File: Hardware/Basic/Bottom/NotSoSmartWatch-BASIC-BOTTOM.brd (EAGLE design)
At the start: 33 x 33 mm, 31 parts, among them U1 AD5242-SO16

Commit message: updated partially through Take 003
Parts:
- added J1: (no value), LinnesLab-Connectors:1X07
- moved R19 53.6 mm to (10.1, -22.2)
- moved R15 53.2 mm to (31.4, -19.7)
- moved R14 52.3 mm to (5.68, -21.0)
- moved C11 50.7 mm to (16.2, -20.1), turned to 90 degrees
- moved R13 50.6 mm to (10.8, -17.4)
- moved IMU1 50.1 mm to (45.1, 40.2)
- moved C1 49.8 mm to (39.9, 40.1)
- moved R21 48.9 mm to (37.3, -17.2)
- moved C14 44.1 mm to (4.16, -12.6)
- moved R17 42.8 mm to (30.3, -6.71)
- moved R18 42.5 mm to (30.3, -8.06), turned to 180 degrees
- moved R20 42.2 mm to (4.85, -15.9)
- moved C16 41.8 mm to (27.8, -16.4)
- moved R22 36.9 mm to (29.9, -12.8), turned to 90 degrees
- moved C15 36.1 mm to (16.1, -16.0)
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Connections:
- removed net LED.CTRL: U$4.8
- removed net PPG: C21.2, OP3.1, U1.14
- removed net TIA: C10.2, C15.1, OP4.1, U1.3
- new net A6/TIA: C10.2, C15.1, J1.5, OP4.1, U1.3
- new net A7/PPG: C21.2, J1.7, OP3.1, U1.14
- new net D29/LED.CTRL: J1.6, U$4.8
- net 3.3V: now also J1.2
- net GND: now also J1.1
- net SCL: now also J1.3
- net SDA: now also J1.4
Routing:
- net N$19: track 0.00 -> 18.4 mm
- net G.W2: track 0.00 -> 4.17 mm
- net N$10: track 0.00 -> 3.96 mm
- net GND: track 0.00 -> 3.96 mm, vias 0 -> 2
- net A7/PPG: track 0.00 -> 2.45 mm
- net N$20: track 0.00 -> 1.75 mm
- net VREF: track 0.00 -> 1.27 mm
- added copper zone on layer 16, net GND

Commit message: still working through Take 003
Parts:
- J1: device LinnesLab-Connectors:1X07 -> LinnesLab-Connectors:1X07_1.27MM
- moved R19 42.1 mm to (32.2, 13.6), turned to 270 degrees
- moved R21 41.5 mm to (26.7, 23.0)
- moved R15 41.0 mm to (26.7, 21.0), turned to 180 degrees
- moved IMU1 40.6 mm to (6.54, 27.4), turned to 90 degrees
- moved R14 38.1 mm to (29.6, 8.63), turned to 0 degrees
- moved C1 37.6 mm to (6.37, 23.0), turned to 0 degrees
- moved R23 35.7 mm to (30.0, 22.4), turned to 180 degrees
- moved R13 35.4 mm to (32.3, 10.7)
- moved C16 35.0 mm to (26.6, 18.5)
- moved U1 33.9 mm to (11.1, 9.05)
- moved C19 33.4 mm to (30.0, 20.5), turned to 180 degrees
- moved C18 33.1 mm to (5.85, 8.44), turned to 270 degrees
- moved R20 32.5 mm to (29.7, 5.13), turned to 180 degrees
- moved C14 32.1 mm to (29.6, 6.91), turned to 180 degrees
- moved R22 31.4 mm to (30.0, 18.6), turned to 0 degrees
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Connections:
- net 3.3V: now also J1.4; no longer J1.2
- net GND: now also J1.3; no longer J1.1
- net SCL: now also J1.2; no longer J1.3
- net SDA: now also J1.1; no longer J1.4
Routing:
- net A6/TIA: track 0.00 -> 39.3 mm, vias 0 -> 2
- net PD.C: track 0.00 -> 25.8 mm, vias 0 -> 2
- net GND: track 3.96 -> 19.1 mm, vias 2 -> 9
- net A7/PPG: track 2.45 -> 16.1 mm
- net G.W2: track 4.17 -> 15.7 mm, vias 0 -> 2
- net N$13: track 0.00 -> 11.4 mm
- net N$17: track 0.00 -> 6.83 mm
- net N$18: track 0.00 -> 6.40 mm
- net N$15: track 0.00 -> 5.91 mm
- net N$19: track 18.4 -> 22.8 mm
- net N$16: track 0.00 -> 4.20 mm
- net LED.C: track 0.00 -> 3.80 mm
- net SCL: track 0.00 -> 3.64 mm
- net SDA: track 0.00 -> 3.12 mm

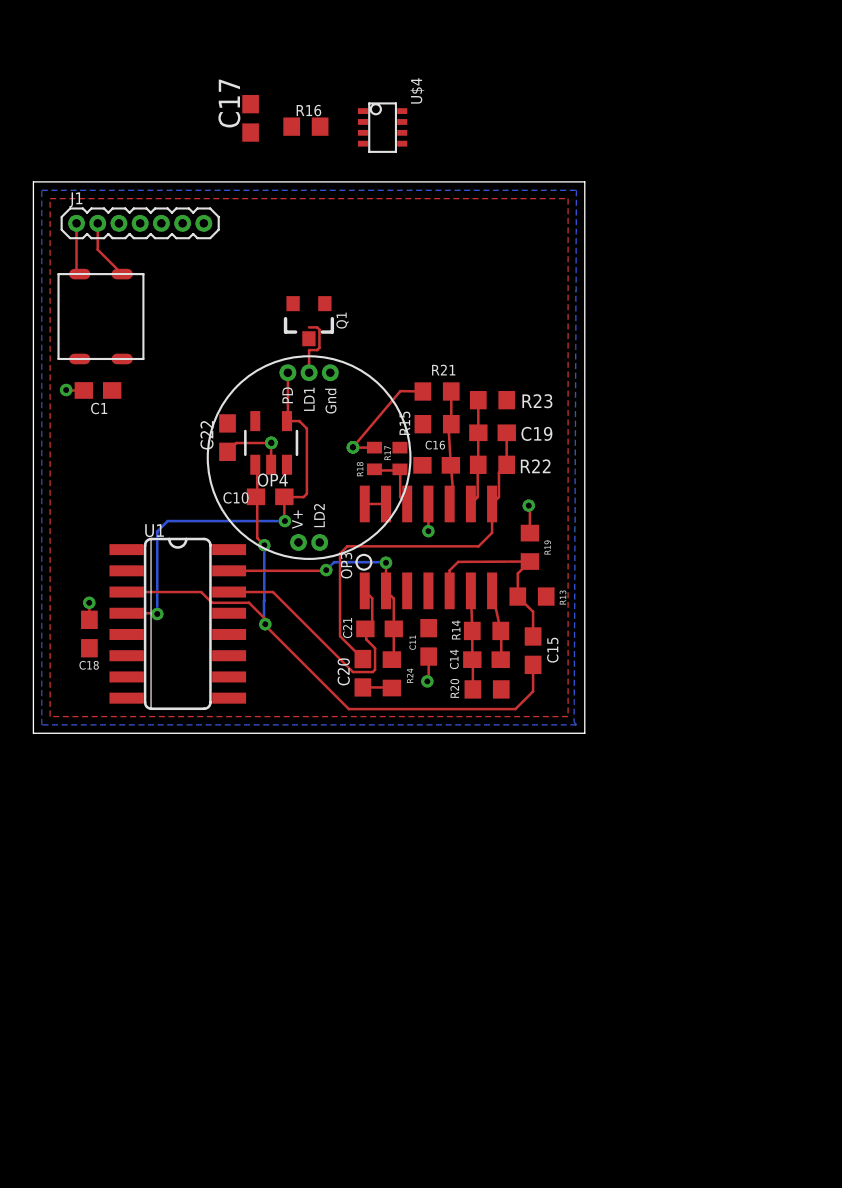
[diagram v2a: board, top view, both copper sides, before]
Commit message: updated through Take 003 - worried I might have isolated polygon
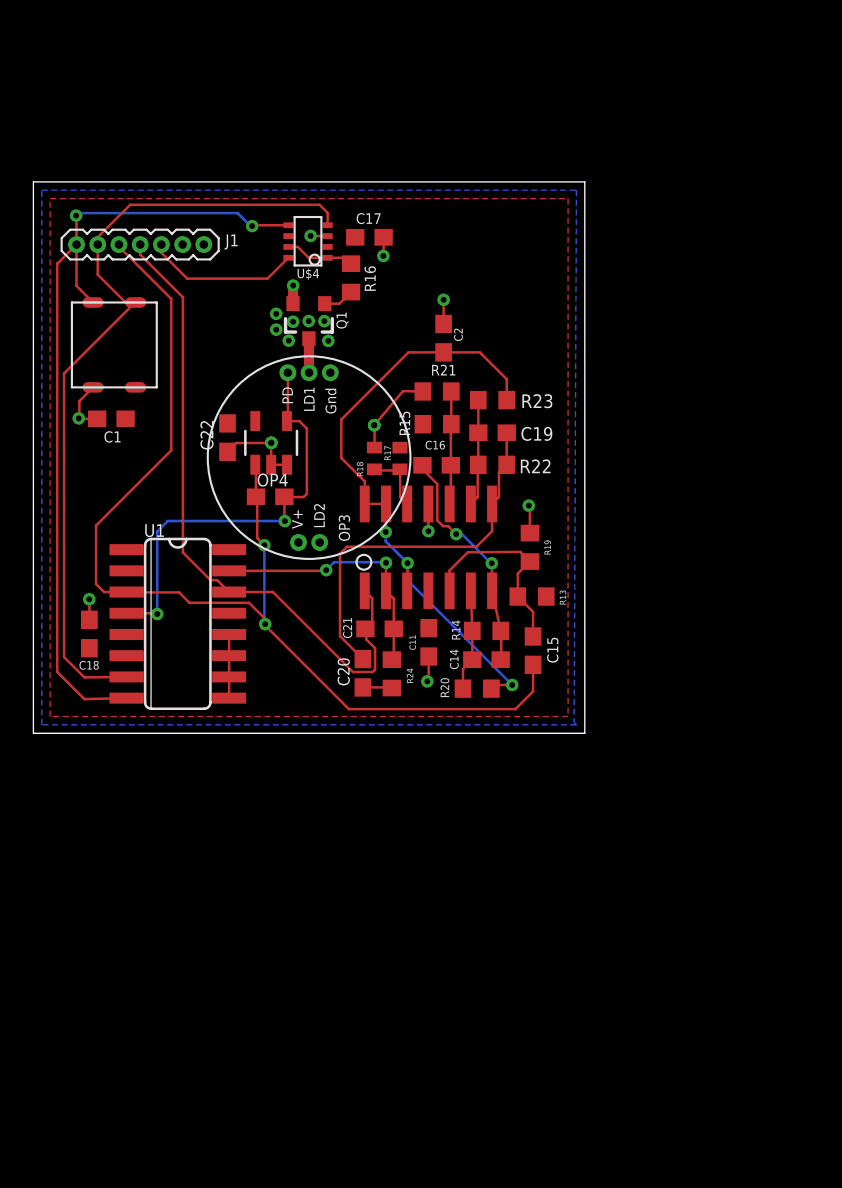
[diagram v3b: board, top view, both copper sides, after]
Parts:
- added C2: 100n, LinnesLab-Passives:C0603
- moved C17 10.1 mm to (22.6, 32.2), turned to 180 degrees
- moved R16 9.44 mm to (21.5, 29.8), turned to 270 degrees
- moved U$4 8.13 mm to (18.9, 31.9), turned to 90 degrees
- moved IMU1 1.88 mm to (7.34, 25.7)
- moved C1 1.88 mm to (7.17, 21.3)
- moved J1 1.27 mm to (5.08, 31.8)
- moved R20 0.59 mm to (29.1, 5.17)
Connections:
- removed net LED: Q1.3
- net 3.3V: now also J1.7; no longer J1.4
- net A6/TIA: now also J1.3; no longer J1.5
- net A7/PPG: now also J1.4; no longer J1.7
- net D29/LED.CTRL: now also J1.5; no longer J1.6
- net GND: now also C2.1, J1.6; no longer J1.3
- net LED.C: now also Q1.3
- net VREF: now also C2.2
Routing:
- net SDA: track 3.12 -> 49.6 mm, vias 0 -> 2
- net SCL: track 3.64 -> 48.0 mm
- net VREF: track 1.27 -> 37.4 mm, vias 0 -> 3
- net A6/TIA: track 39.3 -> 64.8 mm
- net A7/PPG: track 16.1 -> 39.4 mm
- net GND: track 19.1 -> 29.2 mm, vias 9 -> 13
- net N$16: track 4.20 -> 13.9 mm, vias 0 -> 2
- net D29/LED.CTRL: track 0.00 -> 9.24 mm
- net N$9: track 0.00 -> 4.17 mm
- net N$8: track 0.00 -> 1.86 mm
- net LED.C: track 3.80 -> 2.04 mm
